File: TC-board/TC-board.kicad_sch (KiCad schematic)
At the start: 13 parts, among them J1 DB15_Female, J2 PCIE-LP-01-01-F-DV-A-TR, J3 Conn_01x08_Male, J4 Conn_01x02_Male, J5 Conn_01x02_Male

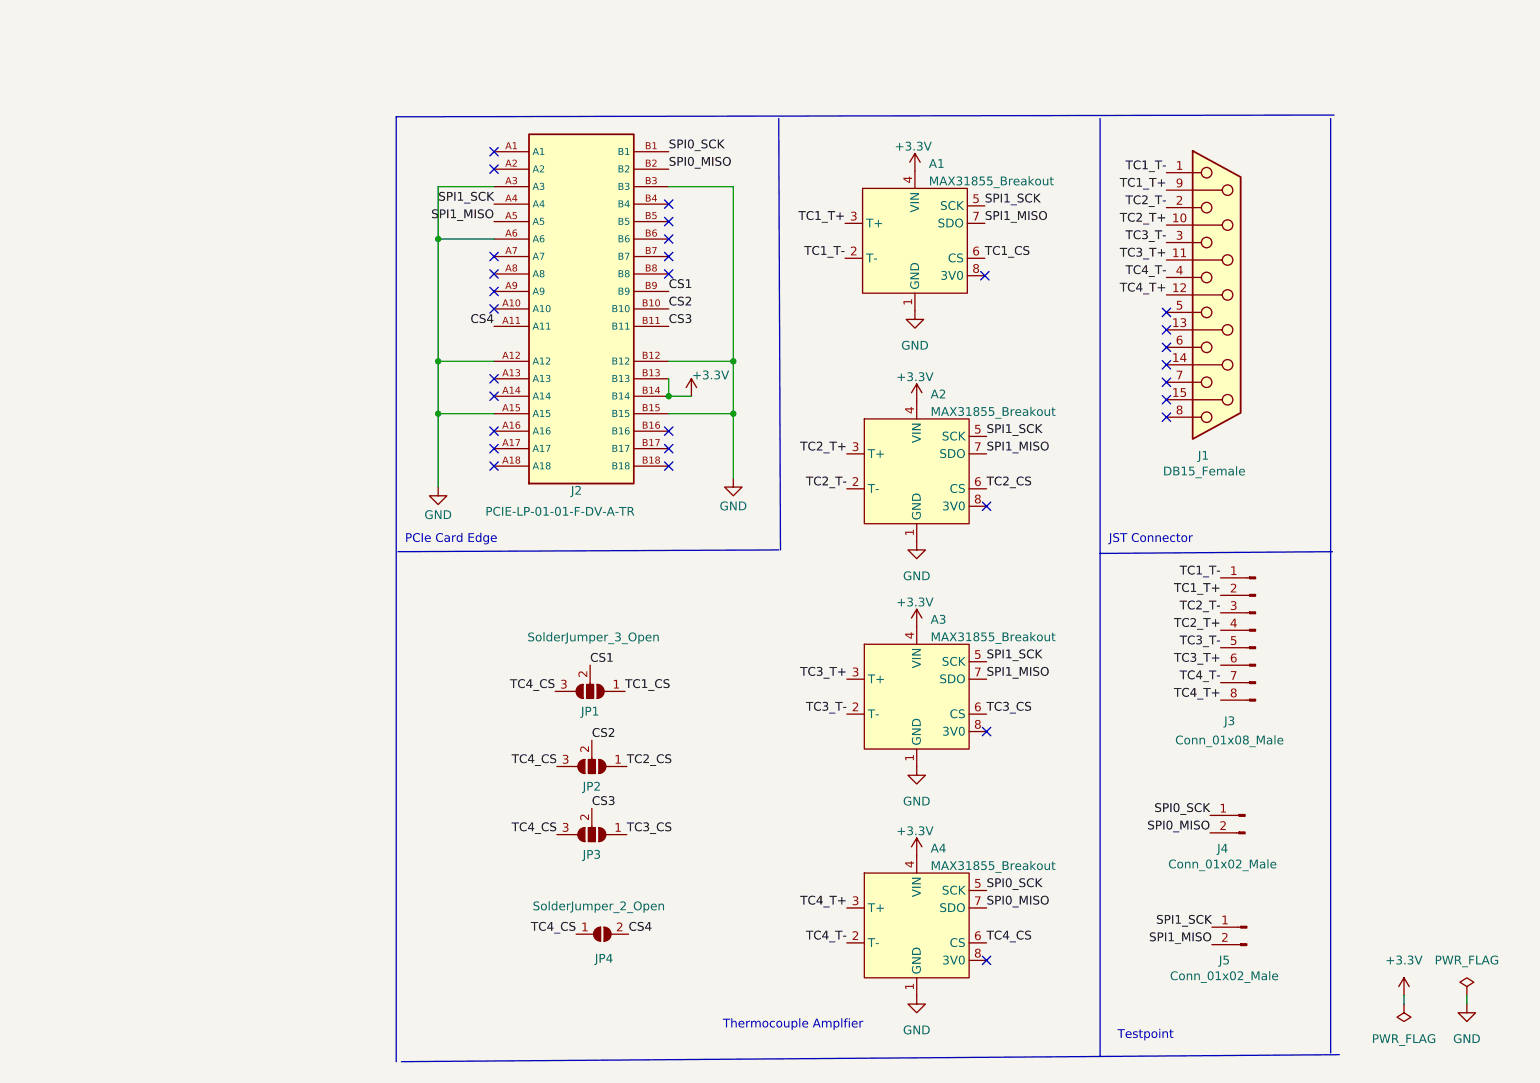
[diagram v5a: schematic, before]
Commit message: PCIe symbol update
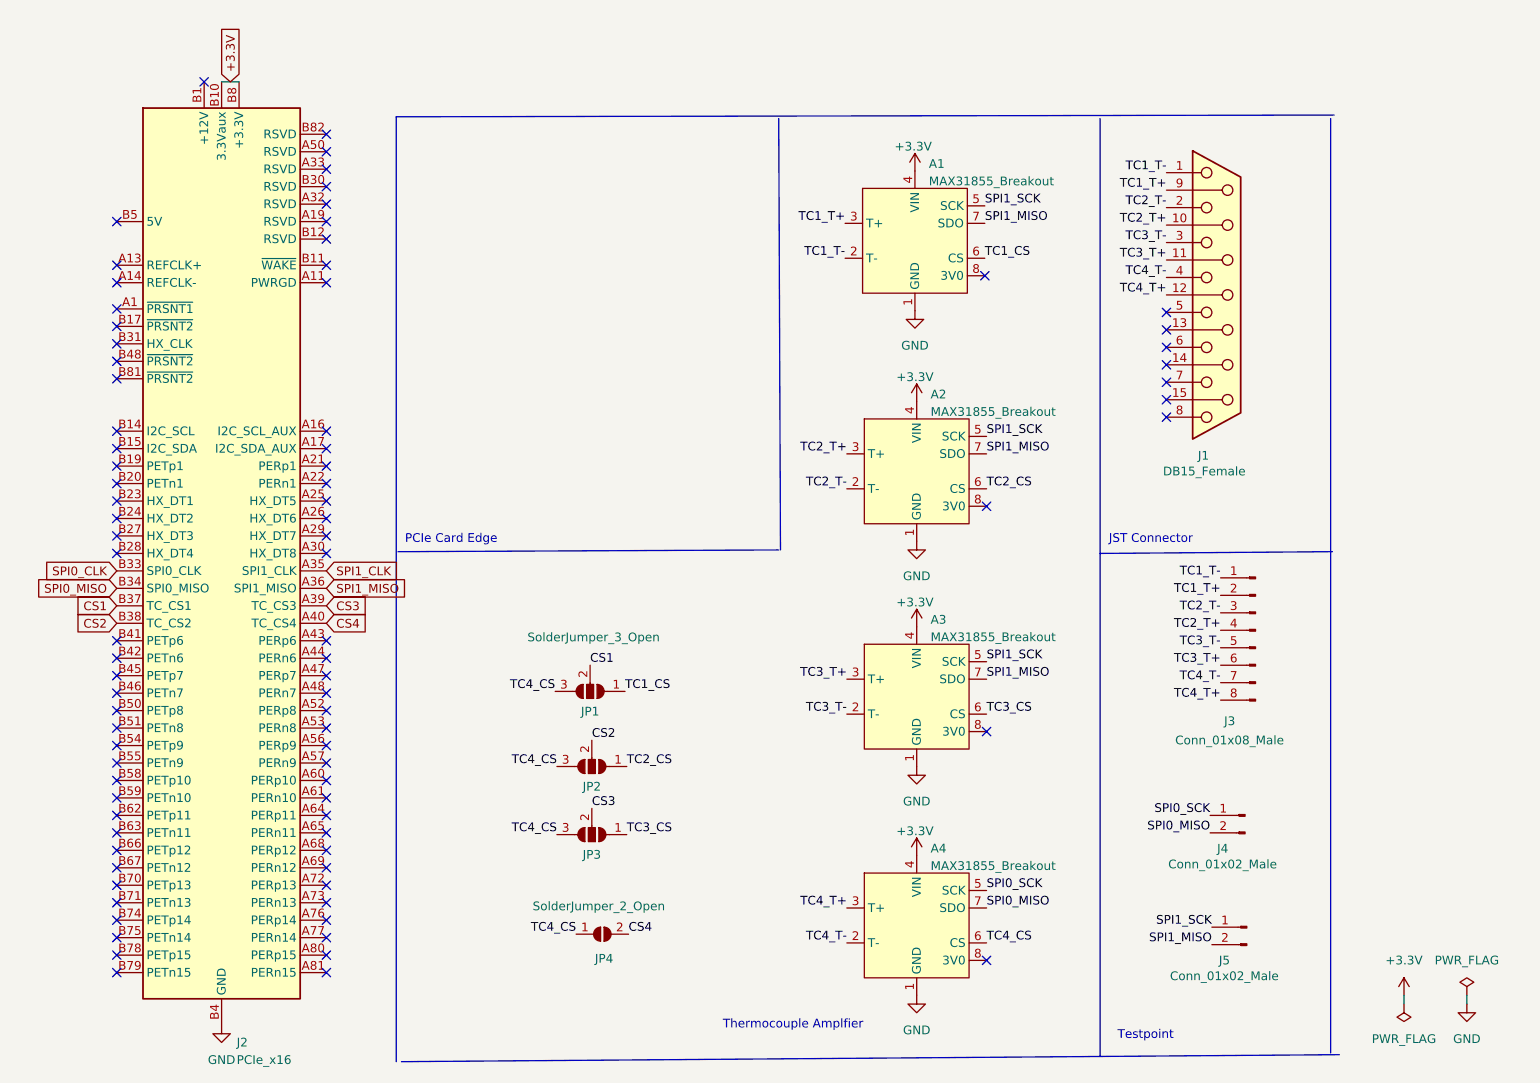
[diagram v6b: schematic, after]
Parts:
- removed J2: PCIE-LP-01-01-F-DV-A-TR, Connector_PCBEdge:BUS_PCIexpress_x1, symbol PCIE_Card_Edge:PCIE-LP-01-01-F-DV-A-TR_(card_edge)
- added J2: PCIe_x16, Connector_PCBEdge:BUS_PCIexpress_x16, symbol PCIe_16x_DAQ:PCIe_x16
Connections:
- net +3.3V: now also J2.A10 (3.3VAux), J2.A8 (3.3V), J2.A9 (+3.3V), J2.B10 (3.3Vaux), J2.B8 (+3.3V), J2.B9 (3.3V)
- net CS1: now also J2.B37 (TC_CS1)
- net CS2: now also J2.B38 (TC_CS2)
- net CS3: now also J2.A39 (TC_CS3)
- net CS4: now also J2.A40 (TC_CS4)
- net GND: now also J2.A12 (GND), J2.A15 (GND), J2.A18 (GND), J2.A20 (GND), J2.A23 (GND), J2.A24 (GND), J2.A27 (GND), J2.A28 (GND), J2.A31 (GND), J2.A34 (GND), J2.A37 (GND), J2.A38 (GND), J2.A4 (GND), J2.A41 (GND), J2.A42 (GND), J2.A45 (GND), J2.A46 (GND), J2.A49 (GND), J2.A51 (GND), J2.A54 (GND), J2.A55 (GND), J2.A58 (GND), J2.A59 (GND), J2.A62 (GND), J2.A63 (GND), J2.A66 (GND), J2.A67 (GND), J2.A7 (GND), J2.A70 (GND), J2.A71 (GND), J2.A74 (GND), J2.A75 (GND), J2.A78 (GND), J2.A79 (GND), J2.A82 (GND), J2.B13 (GND), J2.B16 (GND), J2.B18 (GND), J2.B21 (GND), J2.B22 (GND), J2.B25 (GND), J2.B26 (GND), J2.B29 (GND), J2.B32 (GND), J2.B35 (GND), J2.B36 (GND), J2.B39 (GND), J2.B4 (GND), J2.B40 (GND), J2.B43 (GND), J2.B44 (GND), J2.B47 (GND), J2.B49 (GND), J2.B52 (GND), J2.B53 (GND), J2.B56 (GND), J2.B57 (GND), J2.B60 (GND), J2.B61 (GND), J2.B64 (GND), J2.B65 (GND), J2.B68 (GND), J2.B69 (GND), J2.B7 (GND), J2.B72 (GND), J2.B73 (GND), J2.B76 (GND), J2.B77 (GND), J2.B80 (GND)
- net SPI0_MISO: now also J2.B34 (SPI0_MISO)
- net SPI1_MISO: now also J2.A36 (SPI1_MISO)
- new net: J2.A2 (+12V), J2.A3 (+12V), J2.B1 (+12V), J2.B2 (+12V), J2.B3 (+12V)
- new net: J2.A5 (5V), J2.A6 (5V), J2.B5 (5V), J2.B6 (5V)
- new net SPI0_CLK: J2.B33 (SPI0_CLK)
- new net SPI1_CLK: J2.A35 (SPI1_CLK)
- no-connect marks 30 -> 85

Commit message: Updates to traces in TC board and updates PCIe connector
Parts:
- J2: footprint Connector_PCBEdge:BUS_PCIexpress_x16 -> PCIe_16x_DAQ:Custom-16x-PCIELock
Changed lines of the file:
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@@
       (effects (font (size 1.27 1.27)) (justify left))
     )
-    (property "Footprint" "Connector_PCBEdge:BUS_PCIexpress_x16" (at 40.64 73.66 0)
+    (property "Footprint" "PCIe_16x_DAQ:Custom-16x-PCIELock" (at 40.64 73.66 0)
       (effects (font (size 1.27 1.27)) hide)
     )
